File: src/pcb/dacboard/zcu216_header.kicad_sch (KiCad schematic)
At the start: 9 parts, among them J10 Conn_02x17_Odd_Even, J11 Conn_02x17_Odd_Even, J12 Conn_02x12_Odd_Even, J13 Conn_02x12_Odd_Even, J16 Conn_02x17_Odd_Even, J5 Conn_02x12_Odd_Even, J7 Conn_02x06_Odd_Even, J8 Conn_02x06_Odd_Even, J9 Conn_02x17_Odd_Even

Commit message: dacboard routing
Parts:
- J10, J11, J16, J9: footprint (none) -> Connector_PinHeader_2.00mm:PinHeader_2x17_P2.00mm_Vertical
- J12, J13, J5: footprint (none) -> Connector_PinHeader_2.54mm:PinHeader_2x12_P2.54mm_Vertical
- J7, J8: footprint (none) -> Connector_PinHeader_2.54mm:PinHeader_2x06_P2.54mm_Vertical
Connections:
- net VCCN: now reaches J13.11 (Pin_11)
- net VCCN: now also J13.9 (Pin_9)
- removed net +3V3N: J11.19 (Pin_19), J11.21 (Pin_21), J7.11 (Pin_11), J7.12 (Pin_12), J8.11 (Pin_11), J8.12 (Pin_12), J9.32 (Pin_32)
- no-connect marks 50 -> 55

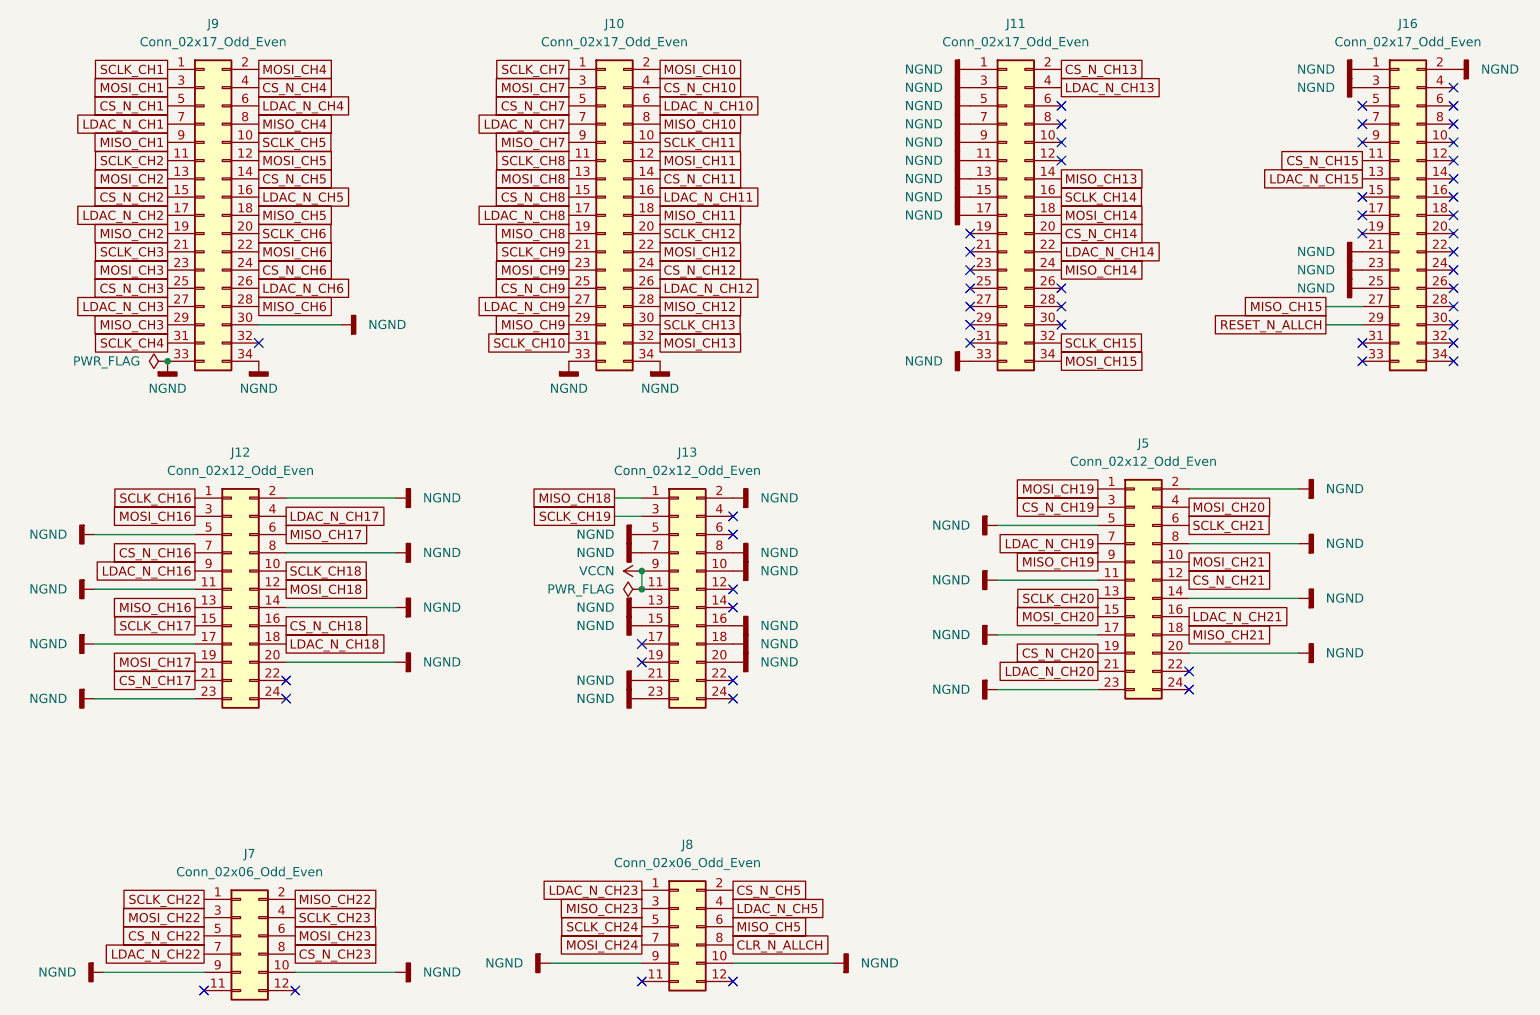
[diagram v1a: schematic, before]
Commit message: finished routing fpga connections
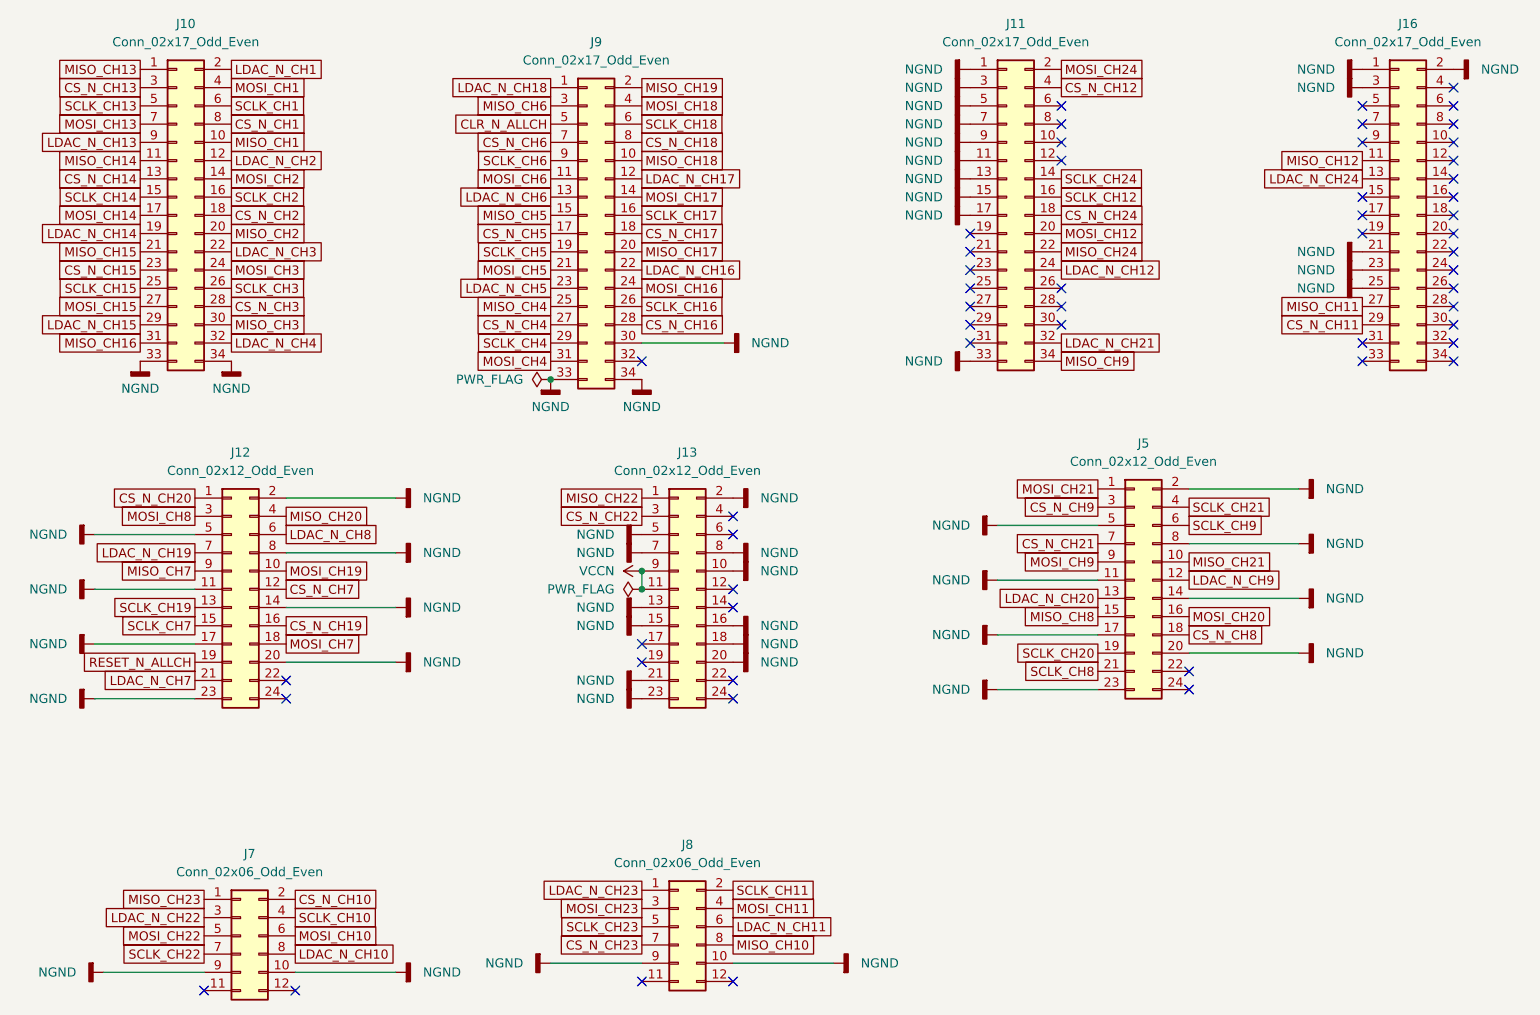
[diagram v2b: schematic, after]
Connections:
- net CLR_N_ALLCH: now also J9.5 (Pin_5); no longer J8.8 (Pin_8)
- net CS_N_CH1: now also J10.8 (Pin_8); no longer J9.5 (Pin_5)
- net CS_N_CH10: now also J7.2 (Pin_2); no longer J10.4 (Pin_4)
- net CS_N_CH11: now also J16.29 (Pin_29); no longer J10.14 (Pin_14)
- net CS_N_CH12: now also J11.4 (Pin_4); no longer J10.24 (Pin_24)
- net CS_N_CH13: now also J10.3 (Pin_3); no longer J11.2 (Pin_2)
- net CS_N_CH14: now also J10.13 (Pin_13); no longer J11.20 (Pin_20)
- net CS_N_CH15: now also J10.23 (Pin_23); no longer J16.11 (Pin_11)
- net CS_N_CH16: now also J9.28 (Pin_28); no longer J12.7 (Pin_7)
- net CS_N_CH17: now also J9.18 (Pin_18); no longer J12.21 (Pin_21)
- net CS_N_CH18: now also J9.8 (Pin_8); no longer J12.16 (Pin_16)
- net CS_N_CH19: now also J12.16 (Pin_16); no longer J5.3 (Pin_3)
- net CS_N_CH2: now also J10.18 (Pin_18); no longer J9.15 (Pin_15)
- net CS_N_CH20: now also J12.1 (Pin_1); no longer J5.19 (Pin_19)
- net CS_N_CH21: now also J5.7 (Pin_7); no longer J5.12 (Pin_12)
- net CS_N_CH22: now also J13.3 (Pin_3); no longer J7.5 (Pin_5)
- net CS_N_CH23: now also J8.7 (Pin_7); no longer J7.8 (Pin_8)
- net CS_N_CH3: now also J10.28 (Pin_28); no longer J9.25 (Pin_25)
- net CS_N_CH4: now also J9.27 (Pin_27); no longer J9.4 (Pin_4)
- net CS_N_CH5: now also J9.17 (Pin_17); no longer J8.2 (Pin_2), J9.14 (Pin_14)
- net CS_N_CH6: now also J9.7 (Pin_7); no longer J9.24 (Pin_24)
- net CS_N_CH7: now also J12.12 (Pin_12); no longer J10.5 (Pin_5)
- net CS_N_CH8: now also J5.18 (Pin_18); no longer J10.15 (Pin_15)
- net CS_N_CH9: now also J5.3 (Pin_3); no longer J10.25 (Pin_25)
- net LDAC_N_CH1: now also J10.2 (Pin_2); no longer J9.7 (Pin_7)
- net LDAC_N_CH10: now also J7.8 (Pin_8); no longer J10.6 (Pin_6)
- net LDAC_N_CH11: now also J8.6 (Pin_6); no longer J10.16 (Pin_16)
- net LDAC_N_CH12: now also J11.24 (Pin_24); no longer J10.26 (Pin_26)
- net LDAC_N_CH13: now also J10.9 (Pin_9); no longer J11.4 (Pin_4)
- net LDAC_N_CH14: now also J10.19 (Pin_19); no longer J11.22 (Pin_22)
- net LDAC_N_CH15: now also J10.29 (Pin_29); no longer J16.13 (Pin_13)
- net LDAC_N_CH16: now also J9.22 (Pin_22); no longer J12.9 (Pin_9)
- net LDAC_N_CH17: now also J9.12 (Pin_12); no longer J12.4 (Pin_4)
- net LDAC_N_CH18: now also J9.1 (Pin_1); no longer J12.18 (Pin_18)
- net LDAC_N_CH19: now also J12.7 (Pin_7); no longer J5.7 (Pin_7)
- net LDAC_N_CH2: now also J10.12 (Pin_12); no longer J9.17 (Pin_17)
- net LDAC_N_CH20: now also J5.13 (Pin_13); no longer J5.21 (Pin_21)
- net LDAC_N_CH21: now also J11.32 (Pin_32); no longer J5.16 (Pin_16)
- net LDAC_N_CH22: now also J7.3 (Pin_3); no longer J7.7 (Pin_7)
- net LDAC_N_CH3: now also J10.22 (Pin_22); no longer J9.27 (Pin_27)
- net LDAC_N_CH4: now also J10.32 (Pin_32); no longer J9.6 (Pin_6)
- net LDAC_N_CH5: now also J9.23 (Pin_23); no longer J8.4 (Pin_4), J9.16 (Pin_16)
- net LDAC_N_CH6: now also J9.13 (Pin_13); no longer J9.26 (Pin_26)
- net LDAC_N_CH7: now also J12.21 (Pin_21); no longer J10.7 (Pin_7)
- net LDAC_N_CH8: now also J12.6 (Pin_6); no longer J10.17 (Pin_17)
- net LDAC_N_CH9: now also J5.12 (Pin_12); no longer J10.27 (Pin_27)
- net MISO_CH1: now also J10.10 (Pin_10); no longer J9.9 (Pin_9)
- net MISO_CH10: now also J8.8 (Pin_8); no longer J10.8 (Pin_8)
- net MISO_CH11: now also J16.27 (Pin_27); no longer J10.18 (Pin_18)
- net MISO_CH12: now also J16.11 (Pin_11); no longer J10.28 (Pin_28)
- net MISO_CH13: now also J10.1 (Pin_1); no longer J11.14 (Pin_14)
- net MISO_CH14: now also J10.11 (Pin_11); no longer J11.24 (Pin_24)
- net MISO_CH15: now also J10.21 (Pin_21); no longer J16.27 (Pin_27)
- net MISO_CH16: now also J10.31 (Pin_31); no longer J12.13 (Pin_13)
- net MISO_CH17: now also J9.20 (Pin_20); no longer J12.6 (Pin_6)
- net MISO_CH18: now also J9.10 (Pin_10); no longer J13.1 (Pin_1)
- net MISO_CH19: now also J9.2 (Pin_2); no longer J5.9 (Pin_9)
- net MISO_CH2: now also J10.20 (Pin_20); no longer J9.19 (Pin_19)
- net MISO_CH21: now also J5.10 (Pin_10); no longer J5.18 (Pin_18)
- net MISO_CH22: now also J13.1 (Pin_1); no longer J7.2 (Pin_2)
- net MISO_CH23: now also J7.1 (Pin_1); no longer J8.3 (Pin_3)
- net MISO_CH3: now also J10.30 (Pin_30); no longer J9.29 (Pin_29)
- net MISO_CH4: now also J9.25 (Pin_25); no longer J9.8 (Pin_8)
- net MISO_CH5: now also J9.15 (Pin_15); no longer J8.6 (Pin_6), J9.18 (Pin_18)
- net MISO_CH6: now also J9.3 (Pin_3); no longer J9.28 (Pin_28)
- net MISO_CH7: now also J12.9 (Pin_9); no longer J10.9 (Pin_9)
- net MISO_CH8: now also J5.15 (Pin_15); no longer J10.19 (Pin_19)
- net MISO_CH9: now also J11.34 (Pin_34); no longer J10.29 (Pin_29)
- net MOSI_CH1: now also J10.4 (Pin_4); no longer J9.3 (Pin_3)
- net MOSI_CH10: now also J7.6 (Pin_6); no longer J10.2 (Pin_2)
- net MOSI_CH11: now also J8.4 (Pin_4); no longer J10.12 (Pin_12)
- net MOSI_CH12: now also J11.20 (Pin_20); no longer J10.22 (Pin_22)
- net MOSI_CH13: now also J10.7 (Pin_7); no longer J10.32 (Pin_32)
- net MOSI_CH14: now also J10.17 (Pin_17); no longer J11.18 (Pin_18)
- net MOSI_CH15: now also J10.27 (Pin_27); no longer J11.34 (Pin_34)
- net MOSI_CH16: now also J9.24 (Pin_24); no longer J12.3 (Pin_3)
- net MOSI_CH17: now also J9.14 (Pin_14); no longer J12.19 (Pin_19)
- net MOSI_CH18: now also J9.4 (Pin_4); no longer J12.12 (Pin_12)
- net MOSI_CH19: now also J12.10 (Pin_10); no longer J5.1 (Pin_1)
- net MOSI_CH2: now also J10.14 (Pin_14); no longer J9.13 (Pin_13)
- net MOSI_CH20: now also J5.16 (Pin_16); no longer J5.15 (Pin_15), J5.4 (Pin_4)
- net MOSI_CH21: now also J5.1 (Pin_1); no longer J5.10 (Pin_10)
- net MOSI_CH22: now also J7.5 (Pin_5); no longer J7.3 (Pin_3)
- net MOSI_CH23: now also J8.3 (Pin_3); no longer J7.6 (Pin_6)
- net MOSI_CH24: now also J11.2 (Pin_2); no longer J8.7 (Pin_7)
- net MOSI_CH3: now also J10.24 (Pin_24); no longer J9.23 (Pin_23)
- net MOSI_CH4: now also J9.31 (Pin_31); no longer J9.2 (Pin_2)
- net MOSI_CH5: now also J9.21 (Pin_21); no longer J9.12 (Pin_12)
- net MOSI_CH6: now also J9.11 (Pin_11); no longer J9.22 (Pin_22)
- net MOSI_CH7: now also J12.18 (Pin_18); no longer J10.3 (Pin_3)
- net MOSI_CH8: now also J12.3 (Pin_3); no longer J10.13 (Pin_13)
- net MOSI_CH9: now also J5.9 (Pin_9); no longer J10.23 (Pin_23)
- net RESET_N_ALLCH: now also J12.19 (Pin_19); no longer J16.29 (Pin_29)
- net SCLK_CH1: now also J10.6 (Pin_6); no longer J9.1 (Pin_1)
- net SCLK_CH10: now also J7.4 (Pin_4); no longer J10.31 (Pin_31)
- net SCLK_CH11: now also J8.2 (Pin_2); no longer J10.10 (Pin_10)
- net SCLK_CH12: now also J11.16 (Pin_16); no longer J10.20 (Pin_20)
- net SCLK_CH13: now also J10.5 (Pin_5); no longer J10.30 (Pin_30)
- net SCLK_CH14: now also J10.15 (Pin_15); no longer J11.16 (Pin_16)
- net SCLK_CH15: now also J10.25 (Pin_25); no longer J11.32 (Pin_32)
- net SCLK_CH16: now also J9.26 (Pin_26); no longer J12.1 (Pin_1)
- net SCLK_CH17: now also J9.16 (Pin_16); no longer J12.15 (Pin_15)
- net SCLK_CH18: now also J9.6 (Pin_6); no longer J12.10 (Pin_10)
- net SCLK_CH19: now also J12.13 (Pin_13); no longer J13.3 (Pin_3)
- net SCLK_CH2: now also J10.16 (Pin_16); no longer J9.11 (Pin_11)
- net SCLK_CH20: now also J5.19 (Pin_19); no longer J5.13 (Pin_13)
- net SCLK_CH21: now also J5.4 (Pin_4); no longer J5.6 (Pin_6)
- net SCLK_CH22: now also J7.7 (Pin_7); no longer J7.1 (Pin_1)
- net SCLK_CH23: now also J8.5 (Pin_5); no longer J7.4 (Pin_4)
- net SCLK_CH24: now also J11.14 (Pin_14); no longer J8.5 (Pin_5)
- net SCLK_CH3: now also J10.26 (Pin_26); no longer J9.21 (Pin_21)
- net SCLK_CH4: now also J9.29 (Pin_29); no longer J9.31 (Pin_31)
- net SCLK_CH5: now also J9.19 (Pin_19); no longer J9.10 (Pin_10)
- net SCLK_CH6: now also J9.9 (Pin_9); no longer J9.20 (Pin_20)
- net SCLK_CH7: now also J12.15 (Pin_15); no longer J10.1 (Pin_1)
- net SCLK_CH8: now also J5.21 (Pin_21); no longer J10.11 (Pin_11)
- net SCLK_CH9: now also J5.6 (Pin_6); no longer J10.21 (Pin_21)
- new net CS_N_CH24: J11.18 (Pin_18)
- new net LDAC_N_CH24: J16.13 (Pin_13)
- new net MISO_CH20: J12.4 (Pin_4)
- new net MISO_CH24: J11.22 (Pin_22)
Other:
- moved on the sheet: J10, J9
